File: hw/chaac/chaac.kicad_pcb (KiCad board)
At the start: 2 copper layers, 80 x 65 mm, 93 parts, among them J1 windrain, J10 Solar Panel, J2 RP_SMA, J3 UART, J4 Battery, J5 Power, J7 AM2315, J8 TC2030-CTX, J9 Therm, Q1 Q_PMOS_GSD, SW1 RST, SW2 RST, U1 MIC550X, U2 NRF52811-QFAA, U3 XBEE_S2C, U5 BMP280, U6 MCP73871, Y1 32.768kHz, Y2 32MHz

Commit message: Progress with chaac base
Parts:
- removed C1: 1uF, Capacitor_SMD:C_0603_1608Metric
- removed C13, C23, C30, C9: 12pF, Capacitor_SMD:C_0402_1005Metric
- removed C15, C21, C22: 0.1uF, Capacitor_SMD:C_0402_1005Metric
- removed C17: 1uF, Capacitor_SMD:C_0402_1005Metric
- removed C18: 100pF, Capacitor_SMD:C_0402_1005Metric
- removed C20, C29, C33: DNP, Capacitor_SMD:C_0402_1005Metric
- removed C24: 4.7uF, Capacitor_SMD:C_0603_1608Metric
- removed C3: 8.2pF, Capacitor_SMD:C_0603_1608Metric
- removed C4: 10uF, Capacitor_SMD:C_0603_1608Metric
- removed F1: 2450FM07A0029T, alvarop:2450FM07A0029T
- removed J2: RP_SMA, Connector_Coaxial:SMA_Samtec_SMA-J-P-H-ST-EM1_EdgeMount
- removed J8: TC2030-CTX, alvarop:TC2030-NL
- removed J9: Therm, Connector_PinHeader_2.54mm:PinHeader_1x02_P2.54mm_Vertical
- removed L1: 15nH, Inductor_SMD:L_0402_1005Metric
- removed L2: 10uH, Inductor_SMD:L_0603_1608Metric
- removed R10, R27: 10k, Resistor_SMD:R_0603_1608Metric
- removed R16: 150k, Resistor_SMD:R_0603_1608Metric
- removed R26: 1k, Resistor_SMD:R_0603_1608Metric
- removed R31: 0, Resistor_SMD:R_0402_1005Metric
- removed the REF** at (175.0, 105.0)
- removed the REF** at (175.0, 50.0)
- removed the REF** at (105.0, 50.0)
- removed the REF** at (105.0, 105.0)
- removed U3: XBEE_S2C, alvarop:XBEE_S2C_TH
- removed Y1: 32.768kHz, Crystal:Crystal_SMD_3215-2Pin_3.2x1.5mm
- removed Y2: 32MHz, Crystal:Crystal_SMD_2016-4Pin_2.0x1.6mm
- added REF**: MountingHole_3.2mm_M3, MountingHole:MountingHole_3.2mm_M3, F.Cu at (168.5, 80.0)
- added REF**: MountingHole_3.2mm_M3, MountingHole:MountingHole_3.2mm_M3, F.Cu at (125.0, 80.0)
- C25: value 4700uF -> 470uF; footprint alvarop:CP_Elec_18x16.5 -> Capacitor_SMD:CP_Elec_8x10
- SW1, SW2: footprint alvarop:PTS645SM43SMTR92 -> alvarop:PTS820J25MSMTRLFS
- U2: value NRF52811-QFAA -> CHAAC_RADIO; footprint Package_DFN_QFN:QFN-48-1EP_6x6mm_P0.4mm_EP4.6x4.6mm -> alvarop:CHAAC_RADIO
- moved J7 71.5 mm to (122.9, 118.5), turned to 90 degrees
- moved J1 66.6 mm to (146.6, 116.0), turned to 0 degrees
- moved R6 48.5 mm to (132.0, 108.0), turned to 0 degrees
- moved R5 46.5 mm to (132.0, 106.5), turned to 0 degrees
- moved R4 45.9 mm to (153.5, 102.0), turned to 90 degrees
- moved R3 44.3 mm to (152.0, 102.0), turned to 270 degrees
- moved C16 44.1 mm to (126.3, 102.8), turned to 270 degrees
- moved U5 43.3 mm to (123.8, 102.8), turned to 270 degrees
- moved C10 42.9 mm to (150.5, 102.0), turned to 90 degrees
- moved C14 40.9 mm to (147.5, 102.0), turned to 270 degrees
- moved R15 40.1 mm to (146.0, 102.0), turned to 270 degrees
- moved C6 40.0 mm to (138.5, 102.0), turned to 270 degrees
- moved R1 39.6 mm to (144.5, 102.0), turned to 90 degrees
- moved C12 39.6 mm to (140.0, 102.0), turned to 270 degrees
- moved C25 39.6 mm to (166.0, 103.5)
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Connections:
- net Net-(U2-Pad19) renamed /P0.23
- net Net-(U2-Pad20) renamed /P0.24
- net Net-(U2-Pad22) renamed /P0.22
- net Net-(U2-Pad23) renamed /P0.19
- net Net-(U2-Pad27) renamed /P0.15
- net Net-(U2-Pad28) renamed /P0.16
- net Net-(U2-Pad29) renamed /P0.13
- net Net-(U2-Pad4) renamed /P0.28-AIN4
- net Net-(U2-Pad5) renamed /P0.29-AIN5
- net Net-(U2-Pad8) renamed /P0.02-AIN0
- R17 pad 1: Net-(J9-Pad2) -> Net-(R17-Pad1)
- U2 pad 1: Net-(C22-Pad1) -> /P0.25
- U2 pad 10: /SDA -> /P0.04-AIN2
- U2 pad 11: /SCL -> /P0.05-AIN3
- U2 pad 12: /BOOT -> /P0.06
- U2 pad 13: +3V3 -> /P0.07
- U2 pad 14: /LED1 -> /P0.08
- U2 pad 15: /LED2 -> /SCL
- U2 pad 16: /UART_TX -> /SDA
- U2 pad 17: /UART_RX -> GND
- U2 pad 18: Net-(U2-Pad18) -> +3V3
- U2 pad 2: Net-(C9-Pad1) -> /P0.26
- U2 pad 21: Net-(U2-Pad21) -> /nRST
- U2 pad 24: /nRST -> /P0.20
- U2 pad 25: /SWCLK -> /P0.17
- U2 pad 26: /SWDIO -> /P0.18
- U2 pad 3: Net-(C13-Pad1) -> /P0.27
- U2 pad 30: Net-(F1-Pad1) -> /P0.14
- U2 pad 31: GND -> /P0.11
- U2 pad 32: Net-(C20-Pad2) -> /P0.12
- U2 pad 6: /WSPEED -> /P0.30-AIN6
- U2 pad 7: /WDIR -> /P0.31-AIN7
- U2 pad 9: /RAIN -> /P0.03-AIN1
- U6 pad 5: Net-(R26-Pad1) -> Net-(R17-Pad1)
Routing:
- net +3V3: track 191.6 -> 0.00 mm, vias 16 -> 0
- net /nRST: track 109.6 -> 0.00 mm, vias 7 -> 0
- net /VSOLAR: track 97.3 -> 0.00 mm, vias 6 -> 0
- net /BATT: track 89.1 -> 0.00 mm, vias 4 -> 0
- net GND: track 85.8 -> 0.00 mm, vias 86 -> 0
- net /SCL: track 79.1 -> 0.00 mm
- net /SDA: track 78.4 -> 0.00 mm, vias 2 -> 0
- net /SNS_3V3: track 78.3 -> 0.00 mm
- net /MCP_VIN: track 76.5 -> 0.00 mm, vias 3 -> 0
- net /WSPEED: track 75.0 -> 0.00 mm
- net /WDIR: track 72.2 -> 0.00 mm
- net /XB_TX: track 69.0 -> 0.00 mm
- net /RAIN: track 67.3 -> 0.00 mm
- net /XB_RX: track 64.3 -> 0.00 mm
- net /BOOT: track 53.9 -> 0.00 mm
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- removed copper zone on B.Cu, net GND
- removed copper zone on F.Cu, net GND
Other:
- board size 80 x 65 mm -> 74.5 x 45.5 mm
- board text added: "Chaac v3.0"
- board text removed: "BATTERY"
- board text removed: "Chaac v2.0"
- board text removed: "PWR"
- board text removed: "T/H"
- board text removed: "TMP"

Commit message: Done routing chaac v3.0 base board?
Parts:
- removed C7: DNP, Capacitor_SMD:C_0603_1608Metric
- removed J5: Power, Connector_PinHeader_2.54mm:PinHeader_1x03_P2.54mm_Vertical
- added REF**: OSHW-Logo2_7.3x6mm_SilkScreen, Symbol:OSHW-Logo2_7.3x6mm_SilkScreen, F.Cu at (114.6, 94.6)
- J10: footprint Connector_PinHeader_2.54mm:PinHeader_1x02_P2.54mm_Vertical -> TerminalBlock_TE-Connectivity:TerminalBlock_TE_282834-2_1x02_P2.54mm_Horizontal
- J7: footprint Connector_PinHeader_2.54mm:PinHeader_1x04_P2.54mm_Vertical -> TerminalBlock_TE-Connectivity:TerminalBlock_TE_282834-4_1x04_P2.54mm_Horizontal
- moved C11 62.0 mm to (115.0, 107.0)
- moved R12 57.0 mm to (118.0, 107.0)
- moved R7 56.5 mm to (116.5, 107.0)
- moved J4 56.5 mm to (117.5, 112.5)
- moved J3 53.4 mm to (168.2, 103.8), turned to 180 degrees
- moved J7 53.1 mm to (176.0, 117.0), turned to 180 degrees
- moved R8 53.0 mm to (174.0, 97.0)
- moved D2 53.0 mm to (116.1, 98.5), turned to 180 degrees
- moved D4 51.9 mm to (116.1, 100.0), turned to 180 degrees
- moved U5 51.1 mm to (174.8, 105.3)
- moved C16 51.1 mm to (177.3, 105.3)
- moved D3 50.9 mm to (116.1, 101.5), turned to 180 degrees
- moved R22 48.9 mm to (119.5, 98.5), turned to 180 degrees
- moved R24 47.8 mm to (119.5, 100.0), turned to 180 degrees
- moved R9 47.5 mm to (174.0, 98.8), turned to 0 degrees
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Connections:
- net /P0.02-AIN0 renamed Net-(U2-Pad8)
- net /P0.03-AIN1 renamed Net-(U2-Pad9)
- net /P0.06 renamed Net-(U2-Pad12)
- net /P0.07 renamed Net-(U2-Pad13)
- net /P0.08 renamed Net-(U2-Pad14)
- net /P0.15 renamed Net-(U2-Pad27)
- net /P0.17 renamed Net-(U2-Pad25)
- net /P0.19 renamed Net-(U2-Pad23)
- net /P0.25 renamed Net-(U2-Pad1)
- net /P0.26 renamed Net-(U2-Pad2)
- net /P0.27 renamed Net-(U2-Pad3)
- net /P0.29-AIN5 renamed Net-(U2-Pad5)
- net /P0.30-AIN6 renamed Net-(U2-Pad6)
- net /P0.31-AIN7 renamed Net-(U2-Pad7)
- J7 pad 1: /SCL -> GND
- J7 pad 2: /SDA -> +3V3
- J7 pad 3: +3V3 -> /SDA
- J7 pad 4: GND -> /SCL
- U2 pad 10: /P0.04-AIN2 -> /VSOLAR
- U2 pad 11: /P0.05-AIN3 -> /BATT
- U2 pad 15: /SCL -> Net-(U2-Pad15)
- U2 pad 16: /SDA -> Net-(U2-Pad16)
- U2 pad 19: /P0.23 -> /SNS_3V3_EN
- U2 pad 20: /P0.24 -> /BOOT
- U2 pad 22: /P0.22 -> /SDA
- U2 pad 24: /P0.20 -> /SCL
- U2 pad 26: /P0.18 -> /LED2
- U2 pad 28: /P0.16 -> /LED1
- U2 pad 29: /P0.13 -> /WSPEED
- U2 pad 30: /P0.14 -> /UART_TX
- U2 pad 31: /P0.11 -> /RAIN
- U2 pad 32: /P0.12 -> /UART_RX
- U2 pad 4: /P0.28-AIN4 -> /WDIR
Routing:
- net +3V3: track 0.00 -> 96.9 mm
- net /VIN: track 0.00 -> 58.7 mm
- net /MCP_VIN: track 0.00 -> 55.0 mm, vias 0 -> 3
- net /SDA: track 0.00 -> 52.0 mm
- net /SCL: track 0.00 -> 50.7 mm
- net GND: track 0.00 -> 40.1 mm, vias 0 -> 35
- net /VBATT: track 0.00 -> 30.0 mm
- net /WDIR: track 0.00 -> 29.0 mm
- net /VSOLAR: track 0.00 -> 28.1 mm
- net /BATT: track 0.00 -> 23.7 mm
- net /UART_RX: track 0.00 -> 22.2 mm
- net /UART_TX: track 0.00 -> 21.7 mm
- net /nRST: track 0.00 -> 19.6 mm, vias 0 -> 2
- net /WSPEED: track 0.00 -> 17.6 mm
- net /RAIN: track 0.00 -> 17.5 mm
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- added copper zone on B.Cu, net GND
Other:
- board text removed: "SOLAR PANEL"
- board text removed: "VIN"

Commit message: re-annotated schematic/board
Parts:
- renumbered C2 to C1, C16 to C10, C25 to C11, C26 to C12, C27 to C13, C28 to C14, C12 to C2, C10 to C3, C6 to C4, C14 to C5, C5 to C6, C19 to C7, C11 to C8, C8 to C9, D5 to D1, D6 to D2, D1 to D3, D2 to D4, D3 to D5, D4 to D6, J7 to J2, J4 to J3, J10 to J4, J3 to J5, R5 to R1, R25 to R10, R30 to R11, R7 to R12, R12 to R13, R28 to R14, R29 to R15, R8 to R16, R9 to R17, R17 to R18, R18 to R19, R6 to R2, R19 to R20, R20 to R21, R21 to R22, R22 to R23, R23 to R24, R24 to R25, R2 to R3, R1 to R4, R3 to R5, R4 to R6, R15 to R7, R11 to R8, R13 to R9, SW2 to SW1, SW1 to SW2, U5 to U3, U6 to U4

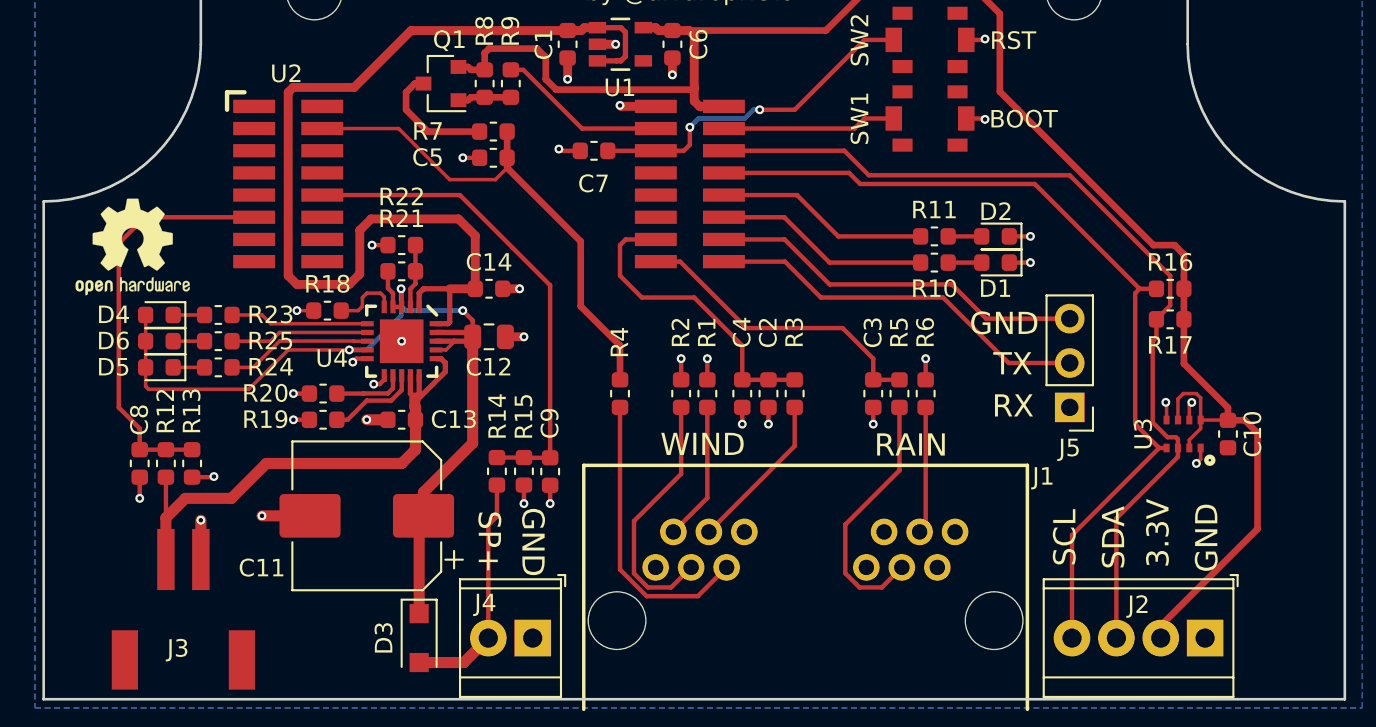
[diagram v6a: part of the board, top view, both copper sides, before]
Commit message: Fixed DRC errors and added url
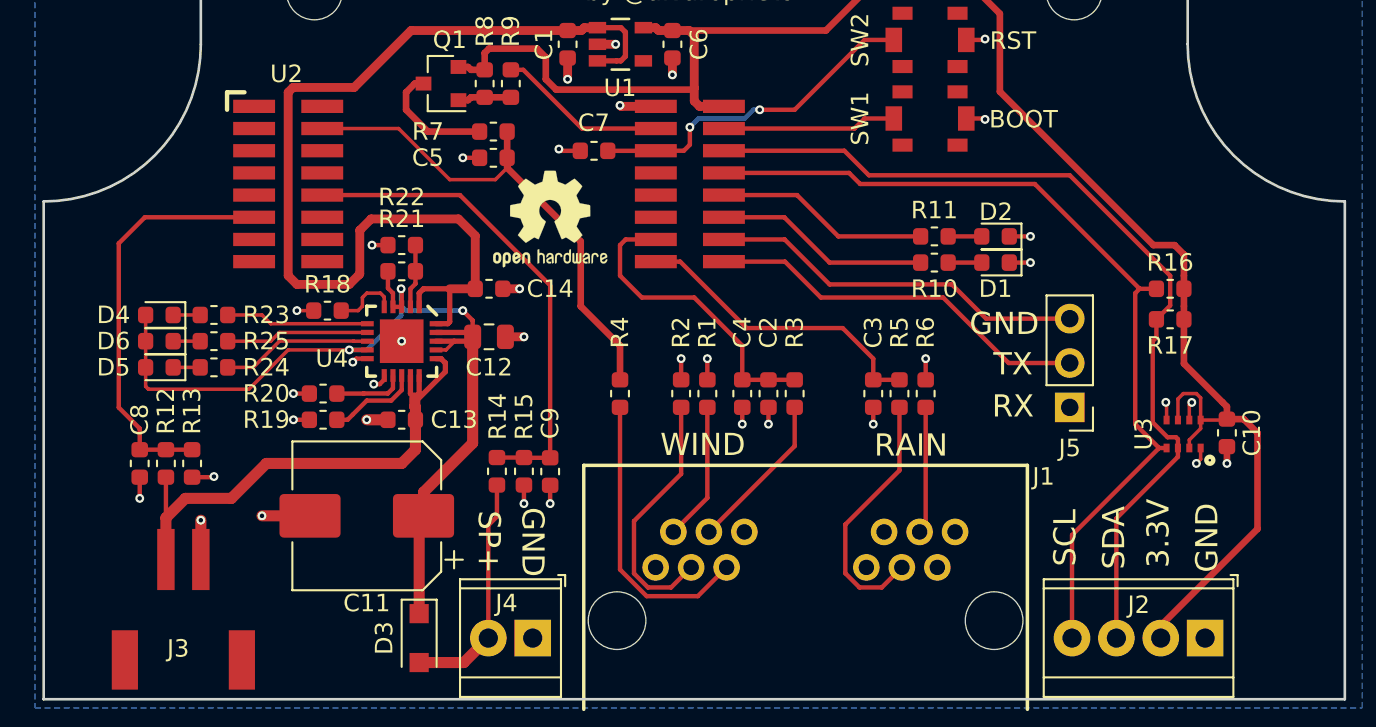
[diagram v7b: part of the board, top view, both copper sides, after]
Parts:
- moved REF** 24.0 mm to (138.5, 93.0)
- moved R23 0.25 mm to (119.2, 98.5)
- moved R24 0.25 mm to (119.2, 101.5)
- moved R25 0.25 mm to (119.2, 100.0)
- moved C10 0.09 mm to (177.2, 105.2)
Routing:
- net GND: track 40.1 -> 41.1 mm, vias 35 -> 36
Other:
- board text added: "https://github.com/alvarop/chaac"
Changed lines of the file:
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@@
   (general
     (thickness 1.6)
-    (drawings 82)
-    (tracks 389)
+    (drawings 83)
+    (tracks 392)
     (zones 0)
     (modules 60)
@@
   )
   (module Symbol:OSHW-Logo2_7.3x6mm_SilkScreen (layer F.Cu)
-    (at 114.6 94.6)
+    (at 138.5 93)
     (descr "Open Source Hardware Symbol")
     (tags "Logo Symbol OSHW")
@@
     (tags resistor)
     (attr smd)
-    (fp_text reference R4 (at 2.921 0 270) (layer F.SilkS)
+    (fp_text reference R4 (at 3.5 0 270) (layer F.SilkS)
       (effects (font (size 1 1) (thickness 0.15)))
     )
@@
   )
   (module Capacitor_SMD:C_0603_1608Metric (layer F.Cu)
-    (at 177.31 105.316 270)
+    (at 177.25 105.25 270)
     (descr "Capacitor SMD 0603 (1608 Metric), square (rectangular) end terminal, IPC_7351 nominal, (Body size source: http://www.tortai-tech.com/upload/download/2011102023233369053.pdf), generated with kicad-footprint-generator")
     (tags capacitor)
@@
     (tags capacitor)
     (attr smd)
-    (fp_text reference C14 (at 0 -1.5) (layer F.SilkS)
+    (fp_text reference C14 (at 3.5 0) (layer F.SilkS)
       (effects (font (size 1 1) (thickness 0.15)))
     )
@@
     (tags resistor)
     (attr smd)
-    (fp_text reference R19 (at -3.3 0) (layer F.SilkS)
+    (fp_text reference R19 (at -3.25 0) (layer F.SilkS)
       (effects (font (size 1 1) (thickness 0.15)))
     )
@@
     (tags resistor)
     (attr smd)
-    (fp_text reference R20 (at -3.3 0) (layer F.SilkS)
+    (fp_text reference R20 (at -3.25 0) (layer F.SilkS)
       (effects (font (size 1 1) (thickness 0.15)))
     )
@@
   )
   (module Resistor_SMD:R_0603_1608Metric (layer F.Cu)
-    (at 119.5 98.5 180)
+    (at 119.25 98.5 180)
     (descr "Resistor SMD 0603 (1608 Metric), square (rectangular) end terminal, IPC_7351 nominal, (Body size source: http://www.tortai-tech.com/upload/download/2011102023233369053.pdf), generated with kicad-footprint-generator")
     (tags resistor)
@@
   )
   (module Resistor_SMD:R_0603_1608Metric (layer F.Cu)
-    (at 119.5 101.5 180)
+    (at 119.25 101.5 180)
     (descr "Resistor SMD 0603 (1608 Metric), square (rectangular) end terminal, IPC_7351 nominal, (Body size source: http://www.tortai-tech.com/upload/download/2011102023233369053.pdf), generated with kicad-footprint-generator")
     (tags resistor)
@@
   )
   (module Resistor_SMD:R_0603_1608Metric (layer F.Cu)
-    (at 119.5 100 180)
+    (at 119.25 100 180)
     (descr "Resistor SMD 0603 (1608 Metric), square (rectangular) end terminal, IPC_7351 nominal, (Body size source: http://www.tortai-tech.com/upload/download/2011102023233369053.pdf), generated with kicad-footprint-generator")
     (tags resistor)
@@
     (tags capacitor)
     (attr smd)
-    (fp_text reference C7 (at 0.0125 -1.9) (layer F.SilkS)
+    (fp_text reference C7 (at 0.0125 1.6) (layer F.SilkS)
       (effects (font (size 1 1) (thickness 0.15)))
     )
@@
     (tags "capacitor electrolytic")
     (attr smd)
-    (fp_text reference C11 (at 6 -3 180) (layer F.SilkS)
+    (fp_text reference C11 (at 0 -5) (layer F.SilkS)
       (effects (font (size 1 1) (thickness 0.15)))
     )
@@
     (descr "Terminal Block TE 282834-2, 2 pins, pitch 2.54mm, size 5.54x6.5mm^2, drill diamater 1.1mm, pad diameter 2.1mm, see http://www.te.com/commerce/DocumentDelivery/DDEController?Action=showdoc&DocId=Customer+Drawing%7F282834%7FC1%7Fpdf%7FEnglish%7FENG_CD_282834_C1.pdf, script-generated using https://github.com/pointhi/kicad-footprint-generator/scripts/TerminalBlock_TE-Connectivity")
     (tags "THT Terminal Block TE 282834-2 pitch 2.54mm size 5.54x6.5mm^2 drill 1.1mm pad 2.1mm")
-    (fp_text reference J4 (at 2.7 2) (layer F.SilkS)
+    (fp_text reference J4 (at 1.5 2) (layer F.SilkS)
       (effects (font (size 1 1) (thickness 0.15)))
     )
@@
       (rotate (xyz -90 0 -180))
     )
+  )
+  (gr_text https://github.com/alvarop/chaac (at 147 77) (layer B.SilkS)
+    (effects (font (size 1.5 1.5) (thickness 0.3)) (justify mirror))
   )
   (gr_text BOOT (at 165.6 87.3) (layer F.SilkS)
@@
   (via (at 128.3 94.5) (size 0.508) (drill 0.254) (layers F.Cu B.Cu) (net 1))
   (segment (start 129.2125 94.5) (end 128.3 94.5) (width 0.254) (layer F.Cu) (net 1))
+  (via (at 177.25 107) (size 0.508) (drill 0.254) (layers F.Cu B.Cu) (net 1))
+  (segment (start 177.25 106.0375) (end 177.25 107) (width 0.381) (layer F.Cu) (net 1))
   (segment (start 143.837 82.05) (end 144.55 82.05) (width 0.508) (layer F.Cu) (net 2))
   (segment (start 144.7125 82.2125) (end 145.5 82.2125) (width 0.508) (layer F.Cu) (net 2))
@@
   (segment (start 138.25 85) (end 138.846901 85.596901) (width 0.381) (layer F.Cu) (net 2))
   (segment (start 146.75 82.5) (end 146.4625 82.2125) (width 0.508) (layer F.Cu) (net 2))
-  (segment (start 174.7875 95.0375) (end 174.7875 96.25) (width 0.381) (layer F.Cu) (net 2))
-  (segment (start 174.25 94.5) (end 174.7875 95.0375) (width 0.381) (layer F.Cu) (net 2))
-  (segment (start 173.0375 94.5) (end 174.25 94.5) (width 0.381) (layer F.Cu) (net 2))
-  (segment (start 156.25 80.25) (end 163.25 80.25) (width 0.381) (layer F.Cu) (net 2))
-  (segment (start 163.25 80.25) (end 164.25 81.25) (width 0.381) (layer F.Cu) (net 2))
-  (segment (start 164.25 85.7125) (end 173.0375 94.5) (width 0.381) (layer F.Cu) (net 2))
-  (segment (start 154.2875 82.2125) (end 156.25 80.25) (width 0.381) (layer F.Cu) (net 2))
-  (segment (start 146.4625 82.2125) (end 154.2875 82.2125) (width 0.381) (layer F.Cu) (net 2))
-  (segment (start 164.25 81.25) (end 164.25 85.7125) (width 0.381) (layer F.Cu) (net 2))
-  (segment (start 174.7875 96.25) (end 174.7875 98) (width 0.381) (layer F.Cu) (net 2))
-  (segment (start 174.7875 98) (end 174.7875 101.2875) (width 0.381) (layer F.Cu) (net 2))
-  (segment (start 177.31 103.81) (end 177.31 104.5285) (width 0.381) (layer F.Cu) (net 2))
-  (segment (start 174.7875 101.2875) (end 177.31 103.81) (width 0.381) (layer F.Cu) (net 2))
   (segment (start 174.445 104.516) (end 174.445 103.305) (width 0.2032) (layer F.Cu) (net 2))
   (segment (start 174.445 103.305) (end 174.75 103) (width 0.2032) (layer F.Cu) (net 2))
@@
   (segment (start 175.745 105.005) (end 175.745 104.516) (width 0.2032) (layer F.Cu) (net 2))
   (segment (start 175.095 105.655) (end 175.745 105.005) (width 0.2032) (layer F.Cu) (net 2))
+  (segment (start 163.25 80.25) (end 164.25 81.25) (width 0.381) (layer F.Cu) (net 2))
+  (segment (start 156.25 80.25) (end 163.25 80.25) (width 0.381) (layer F.Cu) (net 2))
+  (segment (start 173.0375 94.5) (end 174.25 94.5) (width 0.381) (layer F.Cu) (net 2))
+  (segment (start 174.25 94.5) (end 174.7875 95.0375) (width 0.381) (layer F.Cu) (net 2))
+  (segment (start 174.7875 95.0375) (end 174.7875 96.25) (width 0.381) (layer F.Cu) (net 2))
+  (segment (start 146.4625 82.2125) (end 154.2875 82.2125) (width 0.381) (layer F.Cu) (net 2))
+  (segment (start 154.2875 82.2125) (end 156.25 80.25) (width 0.381) (layer F.Cu) (net 2))
+  (segment (start 164.25 85.7125) (end 173.0375 94.5) (width 0.381) (layer F.Cu) (net 2))
+  (segment (start 174.7875 98) (end 174.7875 101.2875) (width 0.381) (layer F.Cu) (net 2))
+  (segment (start 174.7875 96.25) (end 174.7875 98) (width 0.381) (layer F.Cu) (net 2))
+  (segment (start 164.25 81.25) (end 164.25 85.7125) (width 0.381) (layer F.Cu) (net 2))
+  (segment (start 177.25 104.4625) (end 177.25 103.75) (width 0.381) (layer F.Cu) (net 2))
+  (segment (start 177.25 103.75) (end 177 103.5) (width 0.381) (layer F.Cu) (net 2))
+  (segment (start 174.7875 101.2875) (end 177 103.5) (width 0.381) (layer F.Cu) (net 2))
   (segment (start 173.46 116.29) (end 173.46 117) (width 0.381) (layer F.Cu) (net 2))
   (segment (start 179 110.75) (end 173.46 116.29) (width 0.381) (layer F.Cu) (net 2))
+  (segment (start 177.25 104.4625) (end 178.2125 104.4625) (width 0.381) (layer F.Cu) (net 2))
   (segment (start 179 105.25) (end 179 110.75) (width 0.381) (layer F.Cu) (net 2))
-  (segment (start 177.31 104.5285) (end 178.2785 104.5285) (width 0.381) (layer F.Cu) (net 2))
-  (segment (start 178.2785 104.5285) (end 179 105.25) (width 0.381) (layer F.Cu) (net 2))
+  (segment (start 178.2125 104.4625) (end 179 105.25) (width 0.381) (layer F.Cu) (net 2))
   (segment (start 147.5 108.9758) (end 147.5 103.7875) (width 0.254) (layer F.Cu) (net 4))
   (segment (start 145.5558 110.92) (end 147.5 108.9758) (width 0.254) (layer F.Cu) (net 4))
